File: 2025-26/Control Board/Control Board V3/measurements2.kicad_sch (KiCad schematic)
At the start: 14 parts, among them U1 ADS8684IDBTR, U2 INA240A2PWR, U6 INA240A2PWR

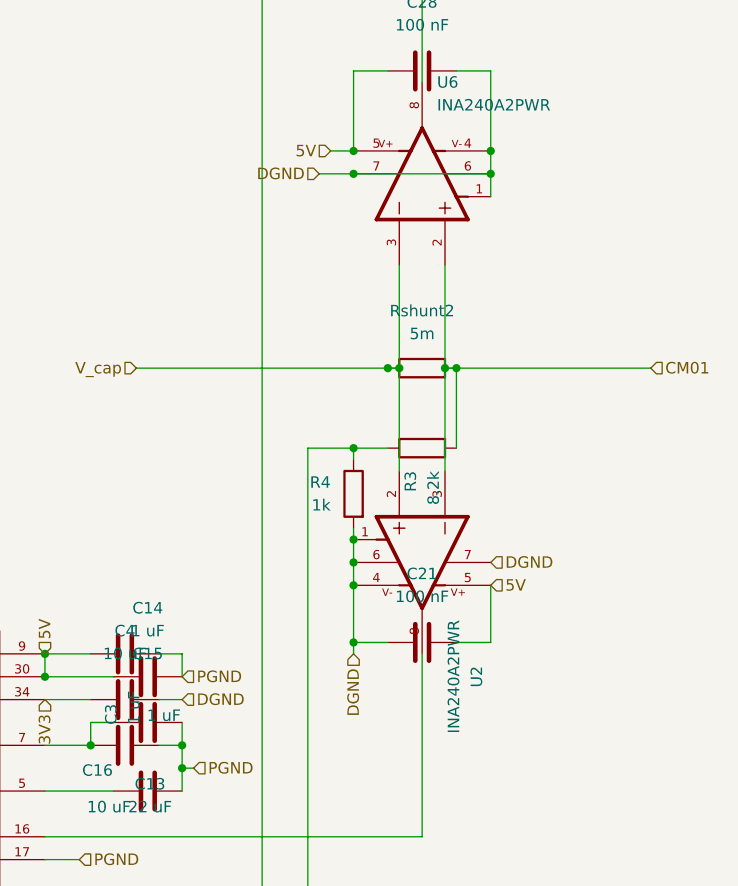
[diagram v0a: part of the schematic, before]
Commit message: so much..
so, not much change to pcbs, mainly the job files are now included.

on the controls side there is a vibe coded mess that needs to be cleaned up. making a checkpoint because i want to see if a separate claude chat can clean up the code first.
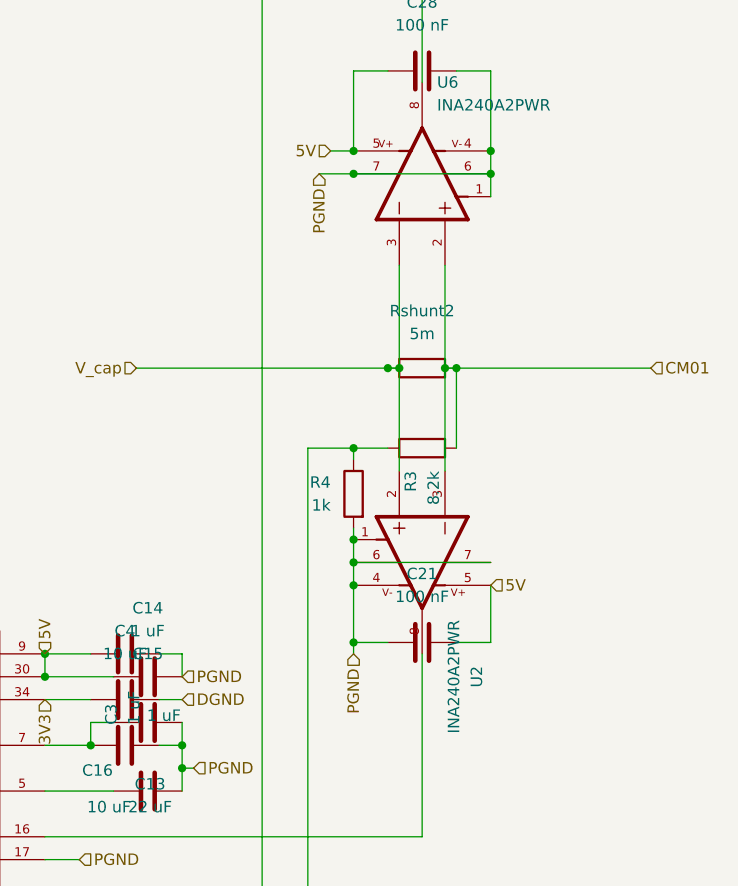
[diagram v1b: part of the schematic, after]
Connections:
- net DGND: no longer C21.1, C28.2, R4.2, U2.1, U2.4, U2.6, U2.7, U6.1, U6.4, U6.6, U6.7
- net PGND: now also C21.1, C28.2, R4.2, U2.1, U2.4, U2.6, U2.7, U6.1, U6.4, U6.6, U6.7
